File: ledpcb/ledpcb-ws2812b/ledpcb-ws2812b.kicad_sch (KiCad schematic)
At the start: 29 parts, among them J1 JST_XA_B03B, J2 JST_XA_B03B, J3 JST_XA_B04B

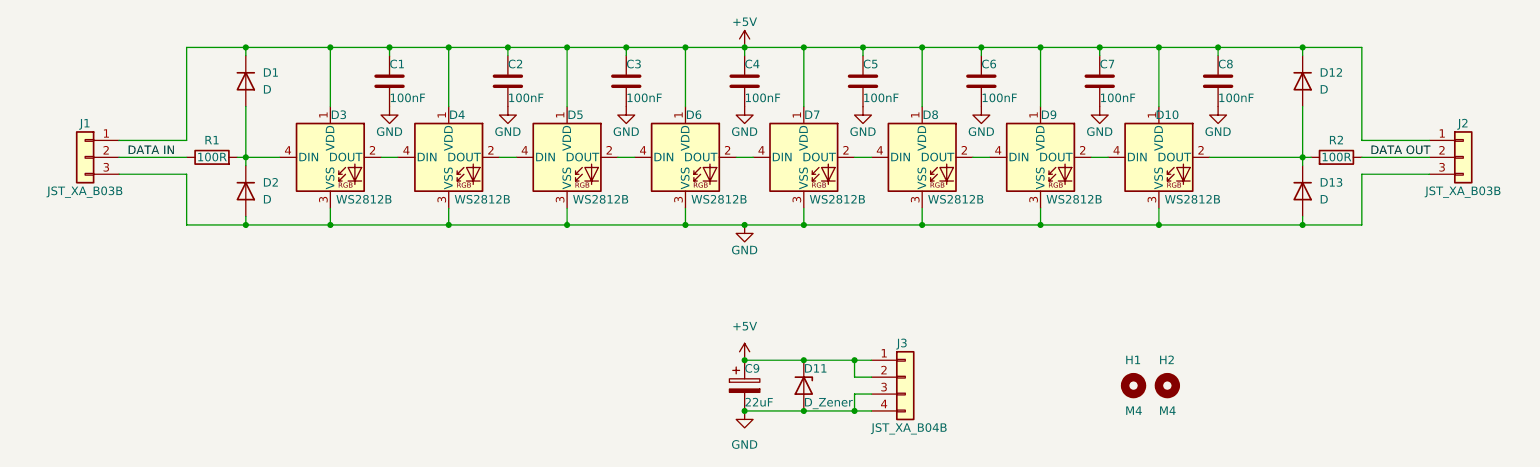
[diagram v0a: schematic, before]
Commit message: Ledpcb designs, ready for ordering.
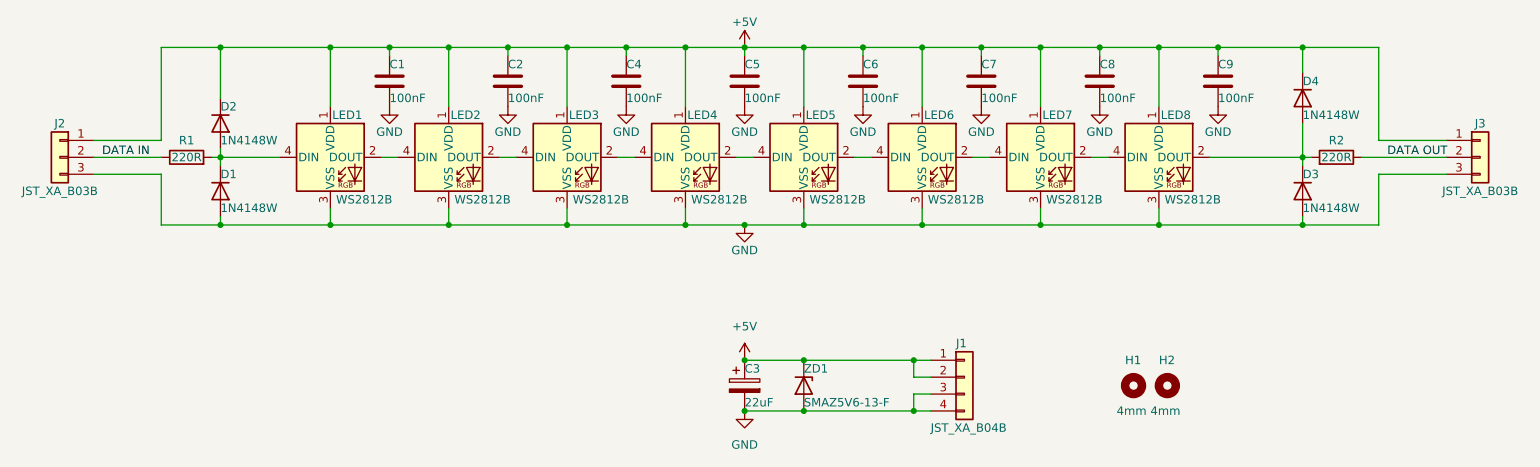
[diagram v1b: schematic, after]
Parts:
- C1, C2: LCSC (none) -> C14663; Package (none) -> 0603
- C3: renamed from C9; LCSC (none) -> C72505; Package (none) -> SMD-6.3x5.4mm
- C4: renamed from C3; LCSC (none) -> C14663; Package (none) -> 0603
- C5: renamed from C4; LCSC (none) -> C14663; Package (none) -> 0603
- C6: renamed from C5; LCSC (none) -> C14663; Package (none) -> 0603
- C7: renamed from C6; LCSC (none) -> C14663; Package (none) -> 0603
- C8: renamed from C7; LCSC (none) -> C14663; Package (none) -> 0603
- C9: renamed from C8; LCSC (none) -> C14663; Package (none) -> 0603
- D1: renamed from D2; value D -> 1N4148W; LCSC (none) -> C81598; Package (none) -> SOD-123
- D2: renamed from D1; value D -> 1N4148W; LCSC (none) -> C81598; Package (none) -> SOD-123
- D3: renamed from D13; value D -> 1N4148W; LCSC (none) -> C81598; Package (none) -> SOD-123
- D4: renamed from D12; value D -> 1N4148W; LCSC (none) -> C81598; Package (none) -> SOD-123
- H1, H2: value M4 -> 4mm; footprint ledpcb:MountingHole_4.3mm_M4 -> ledpcb:MountingHole_3.2mm_M3; now left out of the parts list
- J1: renamed from J3; footprint Connector_JST:JST_XA_B04B-XASK-1-A_1x04_P2.50mm_Vertical -> ledpcb:JST_XA_B04B-XASK-1-A_1x04_P2.50mm_Vertical; LCSC (none) -> C264994; Package (none) -> CONN-TH_B04B-XASK-1_LF_SN
- J2: renamed from J1; footprint Connector_JST:JST_XA_B03B-XASK-1-A_1x03_P2.50mm_Vertical -> ledpcb:JST_XA_B03B-XASK-1-A_1x03_P2.50mm_Vertical; LCSC (none) -> C264992; Package (none) -> CONN-TH_B03B-XASK-1-A_LF_SN
- J3: renamed from J2; footprint Connector_JST:JST_XA_B03B-XASK-1-A_1x03_P2.50mm_Vertical -> ledpcb:JST_XA_B03B-XASK-1-A_1x03_P2.50mm_Vertical; LCSC (none) -> C264992; Package (none) -> CONN-TH_B03B-XASK-1-A_LF_SN
- LED1: renamed from D3; LCSC (none) -> C2761795; Package (none) -> SMD,5x5mm
- LED2: renamed from D4; LCSC (none) -> C2761795; Package (none) -> SMD,5x5mm
- LED3: renamed from D5; LCSC (none) -> C2761795; Package (none) -> SMD,5x5mm
- LED4: renamed from D6; LCSC (none) -> C2761795; Package (none) -> SMD,5x5mm
- LED5: renamed from D7; LCSC (none) -> C2761795; Package (none) -> SMD,5x5mm
- LED6: renamed from D8; LCSC (none) -> C2761795; Package (none) -> SMD,5x5mm
- LED7: renamed from D9; LCSC (none) -> C2761795; Package (none) -> SMD,5x5mm
- LED8: renamed from D10; LCSC (none) -> C2761795; Package (none) -> SMD,5x5mm
- R1, R2: value 100R -> 220R; LCSC (none) -> C22962; Package (none) -> 0603
- ZD1: renamed from D11; value D_Zener -> SMAZ5V6-13-F; LCSC (none) -> C110526; Package (none) -> SMA
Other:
- moved on the sheet: D1, D2, D4, J1, J2, J3, R1
